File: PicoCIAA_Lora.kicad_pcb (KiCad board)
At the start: 2 copper layers, 47 x 30 mm, 8 parts, among them P1 EDGE_SMA, P3 PWR, P4 MOUNTING_HOLE, P5 MOUNTING_HOLE, P6 IO1, P8 IO3, U1 RFM95

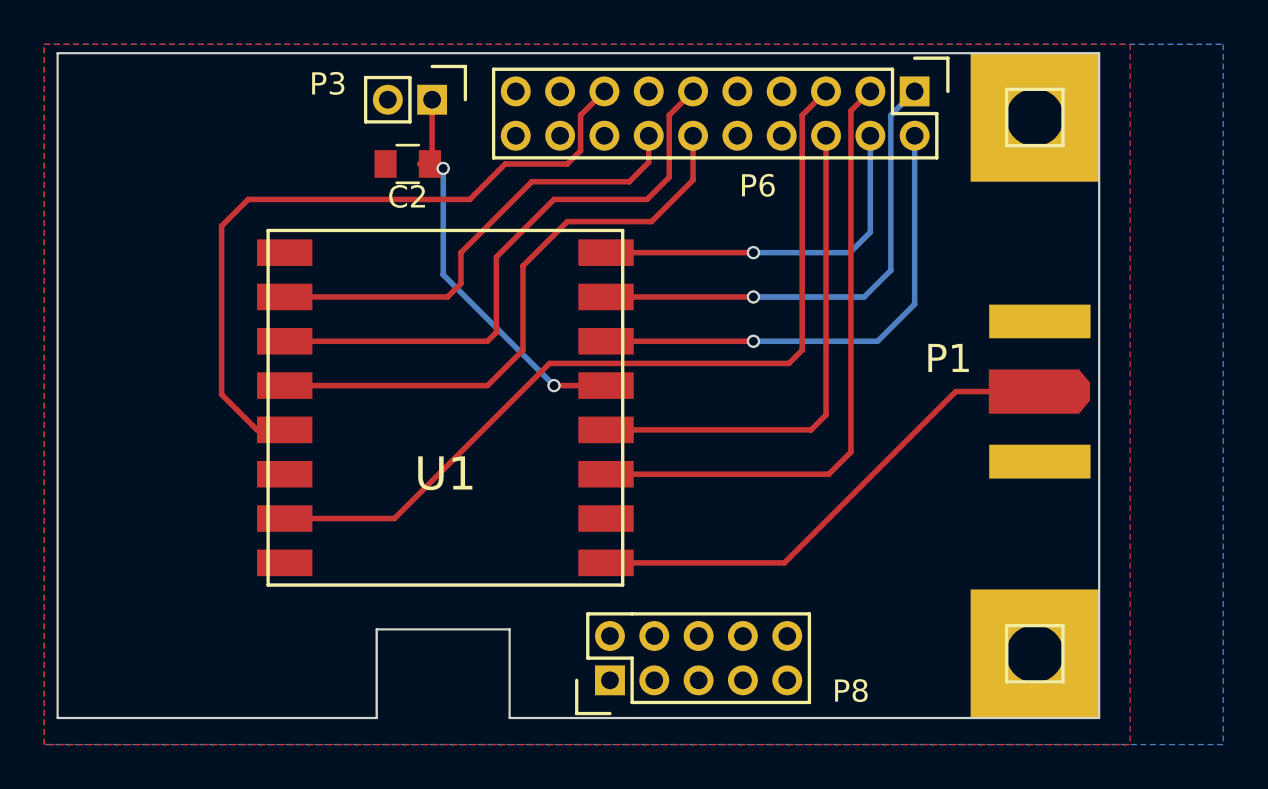
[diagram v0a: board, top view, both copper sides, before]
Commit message: PCB: modificando via y pista
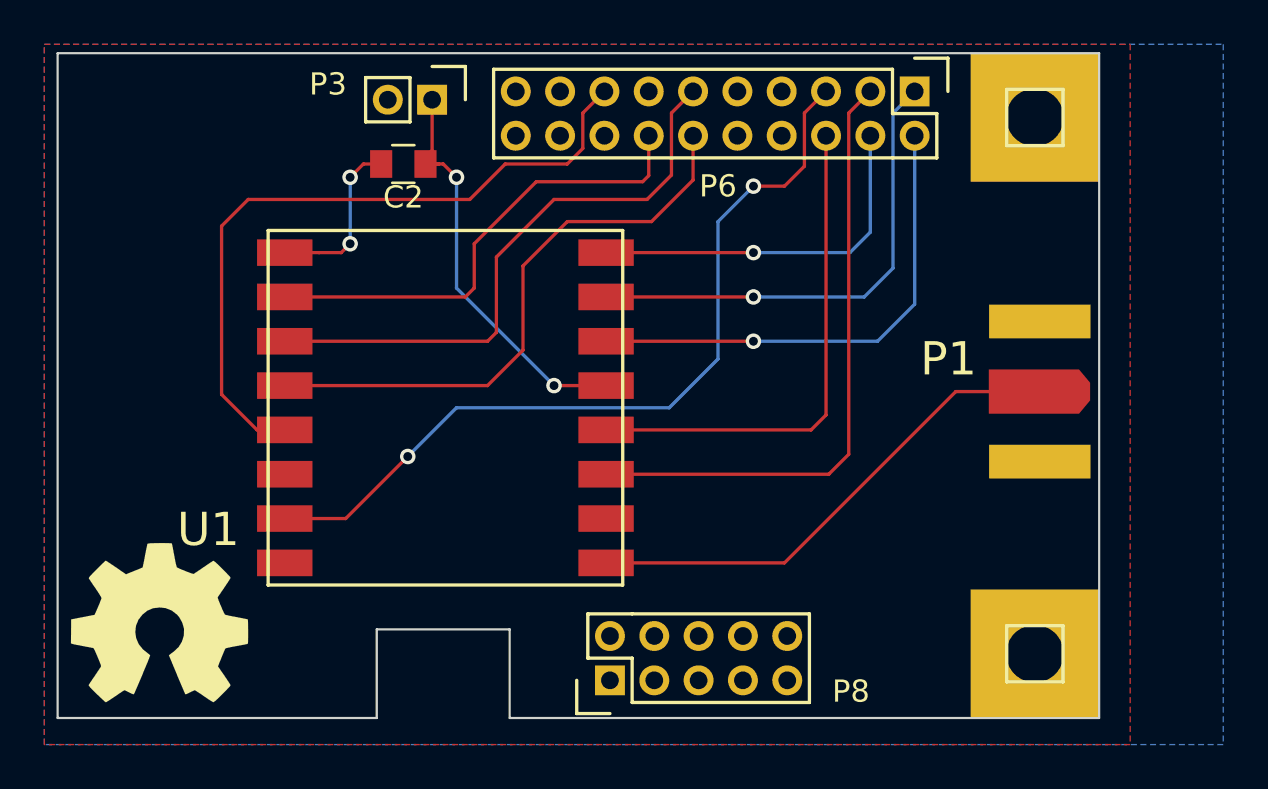
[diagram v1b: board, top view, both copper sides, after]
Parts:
- added G101: Logo_OSHWA, ej2cese:Logo_OSHWA, F.Cu at (57.6, 125.7)
- moved C2 0.20 mm to (68.6, 105.0)
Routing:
- net GND: track 0.00 -> 7.71 mm, vias 0 -> 2
- net /DIO5: track 38.4 -> 37.2 mm, vias 0 -> 2
- net /MISO: track 20.7 -> 21.4 mm
- net +3V3: track 18.2 -> 18.7 mm
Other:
- net class Default: clearance 0 -> 0.15; trace_width 0.25 -> 0.15; via_dia 0.6 -> 0.7
- rule trace_clearance: 0 -> 0.15
- rule trace_min: 0.2 -> 0.15
- rule via_min_drill: 0.3 -> 0.4
- rule via_min_size: 0.4 -> 0.7

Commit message: PCB: Agregando notas de fabricación
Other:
- board text added: "Notas de fabricación * Clearance: 0.15mm * Ancho de pista: 0.15mm * Diámetro vía: 0.70mm * Agujero vía: 0.40mm Nro de capas: 2 Espesor: 1.6mm Grilla de posicionamiento: 0.5mm Grilla de ruteo: 0.1mm"
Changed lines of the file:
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@@
     (area 34.750002 98.6404 108.311905 138.9)
     (thickness 1.6)
-    (drawings 10)
+    (drawings 11)
     (tracks 90)
     (zones 0)
@@
       (xy -2.42316 3.59156)) (layer F.SilkS) (width 0.00254))
   )
+  (gr_text "Notas de fabricación\n* Clearance: 0.15mm\n* Ancho de pista: 0.15mm\n* Diámetro vía: 0.70mm\n* Agujero vía: 0.40mm\n\nNro de capas: 2\nEspesor: 1.6mm\nGrilla de posicionamiento: 0.5mm\nGrilla de ruteo: 0.1mm" (at 110.6 114.3) (layer Dwgs.User)
+    (effects (font (size 1.5 1.5) (thickness 0.3)) (justify left))
+  )
   (dimension 47 (width 0.3) (layer Dwgs.User)
